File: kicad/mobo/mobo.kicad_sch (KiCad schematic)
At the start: 9 parts, among them J1 nice!view, J12 columns, J2 Battery, J4 sensor, J8 rgb, J9 rows, SW1 Power, SW2 Reset, U1 nice!nano v2

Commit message: Dumping everything i need into the combined schematic
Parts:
- removed J1: nice!view, Connector_PinHeader_2.54mm:PinHeader_1x05_P2.54mm_Vertical, symbol Connector:Conn_01x05_Socket
- removed U1: nice!nano v2, ScottoKeebs_MCU:Nice_Nano_V2_Flipped, symbol ScottoKeebs:MCU_Nice_Nano_V2
- added C1: 560pF/680pF, Capacitor_SMD:C_0603_1608Metric_Pad1.08x0.95mm_HandSolder, symbol Device:C_Small
- added C1, C17: 100n, Capacitor_SMD:C_0402_1005Metric, symbol Device:C_Small
- added C12: 1u, Capacitor_SMD:C_0402_1005Metric, symbol Device:C_Small
- added C13, C14, C5, C6, C7: 4u7, Capacitor_SMD:C_0402_1005Metric, symbol Device:C_Small
- added C15, C16: 12p, Capacitor_SMD:C_0402_1005Metric, symbol Device:C_Small
- added C2, C3: 1uF, Capacitor_SMD:C_0603_1608Metric_Pad1.08x0.95mm_HandSolder, symbol Device:C_Small
- added D1: BSD3C051V, Diode_SMD:D_SOD-323, symbol Device:D_TVS
- added F1: 750 mA, Fuse:Fuse_0603_1608Metric, symbol Device:Fuse_Small
- added FB1, FB2: Ferrite_Bead_Small, Resistor_SMD:R_0805_2012Metric_Pad1.20x1.40mm_HandSolder, symbol sharp_memory_display-rescue:Ferrite_Bead_Small-Device
- added J1: Conn_01x05, Connector_PinSocket_2.54mm:PinSocket_1x05_P2.54mm_Vertical, symbol Connector_Generic:Conn_01x05
- added J10: TC2030_SWD, PCM_marbastlib-various:CON_TC2030_outlined, symbol PCM_marbastlib-various:TC2030_SWD
- added J2: HRO_TYPE-C-31-M-14, Connector_USB:USB_C_Receptacle_HRO_TYPE-C-31-M-12, symbol Connector:USB_C_Receptacle_USB2.0
- added J2: Conn_01x10, Connector_FFC-FPC:Hirose_FH12-10S-0.5SH_1x10-1MP_P0.50mm_Horizontal, symbol Connector_Generic:Conn_01x10
- added J3: Battery, PCM_marbastlib-various:Molex_Pico-EZmate_78171-0002_1x02-1MP_P1.20mm_Vertical, symbol Connector_Generic_MountingPin:Conn_01x02_MountingPin
- added L1, L2: BLM15PX121SN1D, Inductor_SMD:L_0402_1005Metric, symbol Device:L_Small
- added L3: 10 uH, Inductor_SMD:L_0603_1608Metric, symbol Device:L_Small
- added LED2: orange, LED_SMD:LED_0402_1005Metric, symbol Device:LED_Small
- added Q2, Q4: 2N7002, Package_TO_SOT_SMD:SOT-23, symbol Transistor_FET:2N7002
- added Q3: AO3401A, Package_TO_SOT_SMD:SOT-23, symbol Transistor_FET:AO3401A
- added R1, R2, R3: 10k, Resistor_SMD:R_0603_1608Metric_Pad0.98x0.95mm_HandSolder, symbol Device:R_Small
- added R1, R18, R19, R2: 5k1, Resistor_SMD:R_0402_1005Metric, symbol Device:R_Small
- added R10, R12: 1k5, Resistor_SMD:R_0402_1005Metric, symbol Device:R_Small
- added R11: 47k, Resistor_SMD:R_0402_1005Metric, symbol Device:R_Small
- added R13: 3k9, Resistor_SMD:R_0402_1005Metric, symbol Device:R_Small
- added R23, R25, R7, R9: 10k, Resistor_SMD:R_0402_1005Metric, symbol Device:R_Small
- added R24, R4: 100R, Resistor_SMD:R_0402_1005Metric, symbol Device:R_Small
- added R3: 100k, Resistor_SMD:R_0402_1005Metric, symbol Device:R_Small
- added SW1: PWR, PCM_marbastlib-various:SW_MSK12C02-HB, symbol Switch:SW_Push_SPDT
- added U1: SRV05-4, Package_TO_SOT_SMD:SOT-23-6, symbol Power_Protection:SRV05-4
- added U10: MAX17048, Package_DFN_QFN:DFN-8-1EP_2x2mm_P0.5mm_EP0.7x1.3mm, symbol marbastlib-various:MAX17048
- added U3: BQ24075, Package_DFN_QFN:VQFN-16-1EP_3x3mm_P0.5mm_EP1.6x1.6mm, symbol Battery_Management:BQ24075RGT
- added U9: nRF52840_E73-2G4M08S1C, E73-2G4M08S1C Model:E73-2G4M08S1C, symbol PCM_marbastlib-various:nRF52840_E73-2G4M08S1C
- added Y1: 32.768 KHz, Crystal:Crystal_SMD_2012-2Pin_2.0x1.2mm, symbol Device:Crystal_Small
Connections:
- net GND: now also C1.2, C1.2, C12.2, C13.2, C14.2, C15.2, C16.2, C17.1, C3.2, C5.2, C6.2, C7.2, D1.1 (A1), FB2.1, J1.1 (Pin_1), J10.5 (GND), J2.9 (Pin_9), J3.2 (Pin_2), J3.MP (MountPin), L2.2, Q2.2 (S), Q4.2 (S), R1.2, R11.2, R12.2, R13.2, R2.2, R25.2, R7.2, R9.2, SW1.3 (C), U1.2 (VN), U10.1 (CTG), U10.4 (GND), U10.6 (QSTRT), U10.9 (GND), U3.17 (VSS), U3.4 (~{CE}), U3.5 (EN2), U3.8 (VSS), U9.21 (GND), U9.24 (GND), U9.5 (GND)
- net RST: now also J10.3 (~{RST}), U9.26 (P0.18/~{RESET})
- net VCC: no longer J8.3 (Pin_3)
- new net: C15.1, U9.11 (P0.00/XL1), Y1.2
- new net: C16.1, U9.13 (P0.01/XL2), Y1.1
- new net: Q4.1 (G), R24.2, R25.1
- new net: F1.1, L1.2
- new net: Q3.1 (G), Q4.3 (D), R23.2
- new net: R9.1, U3.1 (TS)
- new net: R13.1, U3.16 (ISET)
- new net: R10.2, U3.9 (~{CHG})
- new net: LED2.1 (K), R10.1
- new net: Q2.1 (G), R4.2, R7.1
- new net: J2.A5 (CC1), R2.2
- new net: J2.B5 (CC2), R1.2
- new net: R3.1, SW1.1 (A)
- new net +3.3V: C12.1, C3.1, FB1.2, J1.2 (Pin_2), J10.1 (VCC), J2.7 (Pin_7), L3.2, R18.2, R19.2, R3.1, U9.19 (VDD)
- new net +5V: C13.1, C5.1, F1.2, R4.1, U1.5 (VP), U3.13 (IN), U9.27 (VBUS)
- new net +BATT: C17.2, C7.1, J3.1 (Pin_1), R3.2, U10.2 (CELL), U10.3 (VDD), U3.2 (BAT), U3.3 (BAT)
- new net +VSW: C14.1, C6.1, LED2.2 (A), Q3.2 (S), R23.1, U3.10 (OUT), U3.11 (OUT), U3.6 (EN1), U9.23 (VDDH)
- new net ALERT: U10.5 (~{ALRT})
- new net DCCH: L3.1, U9.25 (DCCH)
- new net DISP: C1.1, J2.5 (Pin_5), R3.2
- new net EXTCOMIN: J2.4 (Pin_4), R2.1
- new net EXTMODE: J2.8 (Pin_8), R1.1
- new net Earth: C1.1, D1.2 (A2), J2.A1 (GND), J2.A12 (GND), J2.B1 (GND), J2.B12 (GND), J2.S1 (SHIELD), L2.1
- new net GNDA: C2.2, FB2.2, J2.10 (Pin_10)
- new net GNDPWR: R1.1, R2.1
- new net ILIM: R12.1, U3.12 (ILIM)
- new net SCL: R19.1, U10.7 (SCL), U9.15 (P0.05/AIN3)
- new net SCLK: J1.5 (Pin_5), J2.1 (Pin_1)
- new net SCS: J1.3 (Pin_3), J2.3 (Pin_3)
- new net SDA: R18.1, U10.8 (SDA), U9.22 (P0.07)
- new net SI: J1.4 (Pin_4), J2.2 (Pin_2)
- new net SWDCLK: J10.4 (SWCLK), U9.39 (SWDCLK)
- new net SWDIO: J10.2 (SWDIO), U9.37 (SWDIO)
- new net SYSOFF: Q2.3 (D), SW1.2 (B), U3.15 (SYSOFF)
- new net TMR: R11.1, U3.14 (TMR)
- new net UG_EN: R24.1, U9.36 (P1.00)
- new net UG_LV: U9.34 (P0.22)
- new net UG_PWR: J8.3 (Pin_3), Q3.3 (D)
- new net USB-D+: J2.A6 (D+), J2.B6 (D+), U1.6 (IO4), U9.31 (D+)
- new net USB-D-: J2.A7 (D-), J2.B7 (D-), U1.1 (IO1), U9.29 (D-)
- new net VBUS: J2.A4 (VBUS), J2.A9 (VBUS), J2.B4 (VBUS), J2.B9 (VBUS), L1.1
- new net VDDA: C2.1, FB1.1, J2.6 (Pin_6)
- new net col0: U9.7 (P0.02/AIN0)
- new net col1: U9.4 (P0.28/AIN4)
- new net row0: U9.8 (P0.29/AIN5)
- new net row1: U9.10 (P0.30/AIN6)
- no-connect marks 0 -> 6
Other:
- note added: "Battery management (advanced)"
- note added: "External DCCH inductor for DC-DC HV input mode"
- note added: "External LF crystal for lower idle power"
- note added: "IO connectors"
- note added: "LCD Screen"
- note added: "MCU section (ebyte E73-2G4M08S1C)"
- note added: "SYSOFF 1 (SW1 pos 1): Batt OFF SYSOFF 0 (SW1 pos 3): Batt ON"
- note added: "TMR: (10 x 48 s/kOhm) * 47 kOhm = 22560s = 6.27h ILIM: 1550 AOhm / 1500 Ohm = 1.03 A = 1030 mA ISET: 890 AOhm / 3900 Ohm = 0.228 A = 230 mA EN1: 1, EN2: 0 = 475 mA MAX TS: 10 kOhm to GND = no OTP"
- note added: "USB connectors and protections"
- note added: "Underglow enable"
- note added: "Voltage sensing (advanced)"
- moved on the sheet: J12, J2, J4, J8, J9, SW1, SW2

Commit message: Cleaning up the schematics
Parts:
- removed C1, C17: 100n, Capacitor_SMD:C_0402_1005Metric, symbol Device:C_Small
- removed D1: BSD3C051V, Diode_SMD:D_SOD-323, symbol Device:D_TVS
- removed F1: 750 mA, Fuse:Fuse_0603_1608Metric, symbol Device:Fuse_Small
- removed J1: Conn_01x05, Connector_PinSocket_2.54mm:PinSocket_1x05_P2.54mm_Vertical, symbol Connector_Generic:Conn_01x05
- removed J10: TC2030_SWD, PCM_marbastlib-various:CON_TC2030_outlined, symbol PCM_marbastlib-various:TC2030_SWD
- removed J3: Battery, PCM_marbastlib-various:Molex_Pico-EZmate_78171-0002_1x02-1MP_P1.20mm_Vertical, symbol Connector_Generic_MountingPin:Conn_01x02_MountingPin
- removed L1, L2: BLM15PX121SN1D, Inductor_SMD:L_0402_1005Metric, symbol Device:L_Small
- removed Q2: 2N7002, Package_TO_SOT_SMD:SOT-23, symbol Transistor_FET:2N7002
- removed R18, R19: 5k1, Resistor_SMD:R_0402_1005Metric, symbol Device:R_Small
- removed R3: 100k, Resistor_SMD:R_0402_1005Metric, symbol Device:R_Small
- removed R4: 100R, Resistor_SMD:R_0402_1005Metric, symbol Device:R_Small
- removed R7: 10k, Resistor_SMD:R_0402_1005Metric, symbol Device:R_Small
- removed SW1: Power, Button_Switch_SMD:SW_SPDT_PCM12, symbol ScottoKeebs:Placeholder_Switch
- removed SW1: PWR, PCM_marbastlib-various:SW_MSK12C02-HB, symbol Switch:SW_Push_SPDT
- removed U1: SRV05-4, Package_TO_SOT_SMD:SOT-23-6, symbol Power_Protection:SRV05-4
- removed U10: MAX17048, Package_DFN_QFN:DFN-8-1EP_2x2mm_P0.5mm_EP0.7x1.3mm, symbol marbastlib-various:MAX17048
- added R11, R14, R15, R16, R8: 100R, Resistor_SMD:R_0402_1005Metric, symbol Device:R_Small
- added SW1: Battery, symbol Switch:SW_SPST
- J4: renamed from J12; symbol Connector:Conn_01x07_Socket -> Connector:Conn_01x06_Socket
- J6: renamed from J9; symbol Connector:Conn_01x04_Socket -> Connector:Conn_01x05_Socket
- renumbered C5 to C1, C2 to C10, C16 to C11, C6 to C2, C7 to C3, C12 to C4, C13 to C5, C14 to C6, C1 to C7, C3 to C8, C15 to C9, J2 to J1, J8 to J3, J2 to J5, J4 to J7, L3 to L1, LED2 to LED1, Q3 to Q1, Q4 to Q2, R2 to R1, R23 to R10, R1 to R12, R2 to R13, R24 to R17, R25 to R18, R1 to R2, R9 to R3, R10 to R4, R11 to R5, R12 to R6, R13 to R7, R3 to R9, U3 to U1, U9 to U2
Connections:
- net GNDPWR is gone; now on net GND: R1.1, R2.1
- net VBUS is gone; now on net +5V: J1.A4 (VBUS), J1.A9 (VBUS), J1.B4 (VBUS), J1.B9 (VBUS)
- net VCC is gone; now on net +3.3V: J7.1 (Pin_1)
- net +BATT: now also SW1.2 (B)
- net GND: now also J1.A1 (GND), J1.A12 (GND), J1.B1 (GND), J1.B12 (GND), J2.2 (Pin_2), J3.3 (Pin_3); no longer J2.1 (Pin_1), J3.2 (Pin_2)
- net CS_T: no longer names the net of J7.2 (Pin_2)
- net CS_T: now also R11.2
- removed net Col 6: J4.7 (Pin_7)
- net DISP: no longer names the net of C7.1, J5.5 (Pin_5), R9.2
- removed net Earth: J1.A1 (GND), J1.A12 (GND), J1.B1 (GND), J1.B12 (GND), J1.S1 (SHIELD)
- net IRQ: no longer names the net of J7.5 (Pin_5)
- net IRQ: now also R16.2
- net RGB renamed RGB_PWR
- net RGB_PWR: now also Q1.3 (D)
- net SCK: no longer names the net of J7.4 (Pin_4)
- net SCK: now also R15.2
- net SCL: no longer names the net of U2.15 (P0.05/AIN3)
- net SCLK renamed LCD_CLK
- net SCS renamed LCD_CS
- net SDA: no longer names the net of U2.22 (P0.07)
- net SDIO: no longer names the net of J7.3 (Pin_3)
- net SDIO: now also R14.2
- net SI renamed LCD_IN
- net SWDCLK: no longer names the net of U2.39 (SWDCLK)
- net SWDIO: no longer names the net of U2.37 (SWDIO)
- net SYSOFF: no longer names the net of U1.15 (SYSOFF)
- net UG_EN renamed RGB_ON
- net UG_LV: no longer names the net of U2.34 (P0.22)
- removed net UG_PWR: J3.3 (Pin_3), Q1.3 (D)
- net col0: no longer names the net of U2.7 (P0.02/AIN0)
- net col1: no longer names the net of U2.4 (P0.28/AIN4)
- net row0: no longer names the net of U2.8 (P0.29/AIN5)
- net row1: no longer names the net of U2.10 (P0.30/AIN6)
- new net: J2.1 (Pin_1), SW1.1 (A)
- new net: J3.2 (Pin_2), R8.2
- new net RGB_DATA: R8.1
- new net Row 4: J6.5 (Pin_5)
- new net SENSOR_IRQ: R16.1
- new net SENSOR_SCK: R15.1
- new net SENSOR_SDIO: R14.1
- new net SESOR_CS: R11.1
- no-connect marks 6 -> 5
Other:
- note added: "Battery management"
- note added: "MCU section"
- note added: "USB connector"
- note removed: "Battery management (advanced)"
- note removed: "MCU section (ebyte E73-2G4M08S1C)"
- note removed: "SYSOFF 1 (SW1 pos 1): Batt OFF SYSOFF 0 (SW1 pos 3): Batt ON"
- note removed: "USB connectors and protections"
- note removed: "Voltage sensing (advanced)"
- moved on the sheet: C1, C2, C3, J1, J2, J3, J7, LED1, R1, R2, R3, R4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

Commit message: Replacing the through holes with JST-SH connectors
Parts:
- J2: footprint Connector_JST:JST_ZH_S2B-ZR-SM4A-TF_1x02-1MP_P1.50mm_Horizontal -> Connector_JST:JST_SH_SM02B-SRSS-TB_1x02-1MP_P1.00mm_Horizontal
- J3: footprint Connector_Wuerth:Wuerth_WR-WTB_64800311622_1x03_P1.50mm_Vertical -> Connector_JST:JST_SH_SM03B-SRSS-TB_1x03-1MP_P1.00mm_Horizontal
- J4: footprint Connector_Wuerth:Wuerth_WR-WTB_64800711622_1x07_P1.50mm_Vertical -> Connector_JST:JST_SH_SM06B-SRSS-TB_1x06-1MP_P1.00mm_Horizontal
- J6: footprint Connector_Wuerth:Wuerth_WR-WTB_64800411622_1x04_P1.50mm_Vertical -> Connector_JST:JST_SH_SM05B-SRSS-TB_1x05-1MP_P1.00mm_Horizontal
- J7: footprint Connector_Wuerth:Wuerth_WR-WTB_64800611622_1x06_P1.50mm_Vertical -> Connector_JST:JST_SH_SM06B-SRSS-TB_1x06-1MP_P1.00mm_Horizontal
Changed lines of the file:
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@@
 			)
 		)
-		(property "Footprint" "Connector_Wuerth:Wuerth_WR-WTB_64800711622_1x07_P1.50mm_Vertical"
+		(property "Footprint" "Connector_JST:JST_SH_SM06B-SRSS-TB_1x06-1MP_P1.00mm_Horizontal"
 			(at 223.52 143.51 0)
 			(effects
@@
 			)
 		)
-		(property "Footprint" "Connector_JST:JST_ZH_S2B-ZR-SM4A-TF_1x02-1MP_P1.50mm_Horizontal"
+		(property "Footprint" "Connector_JST:JST_SH_SM02B-SRSS-TB_1x02-1MP_P1.00mm_Horizontal"
 			(at 193.04 62.23 0)
 			(effects
@@
 			)
 		)
-		(property "Footprint" "Connector_Wuerth:Wuerth_WR-WTB_64800311622_1x03_P1.50mm_Vertical"
+		(property "Footprint" "Connector_JST:JST_SH_SM03B-SRSS-TB_1x03-1MP_P1.00mm_Horizontal"
 			(at 224.79 127 0)
 			(effects
@@
 			)
 		)
-		(property "Footprint" "Connector_Wuerth:Wuerth_WR-WTB_64800411622_1x04_P1.50mm_Vertical"
+		(property "Footprint" "Connector_JST:JST_SH_SM05B-SRSS-TB_1x05-1MP_P1.00mm_Horizontal"
 			(at 223.52 162.56 0)
 			(effects
@@
 			)
 		)
-		(property "Footprint" "Connector_Wuerth:Wuerth_WR-WTB_64800611622_1x06_P1.50mm_Vertical"
+		(property "Footprint" "Connector_JST:JST_SH_SM06B-SRSS-TB_1x06-1MP_P1.00mm_Horizontal"
 			(at 223.52 187.96 0)
 			(effects

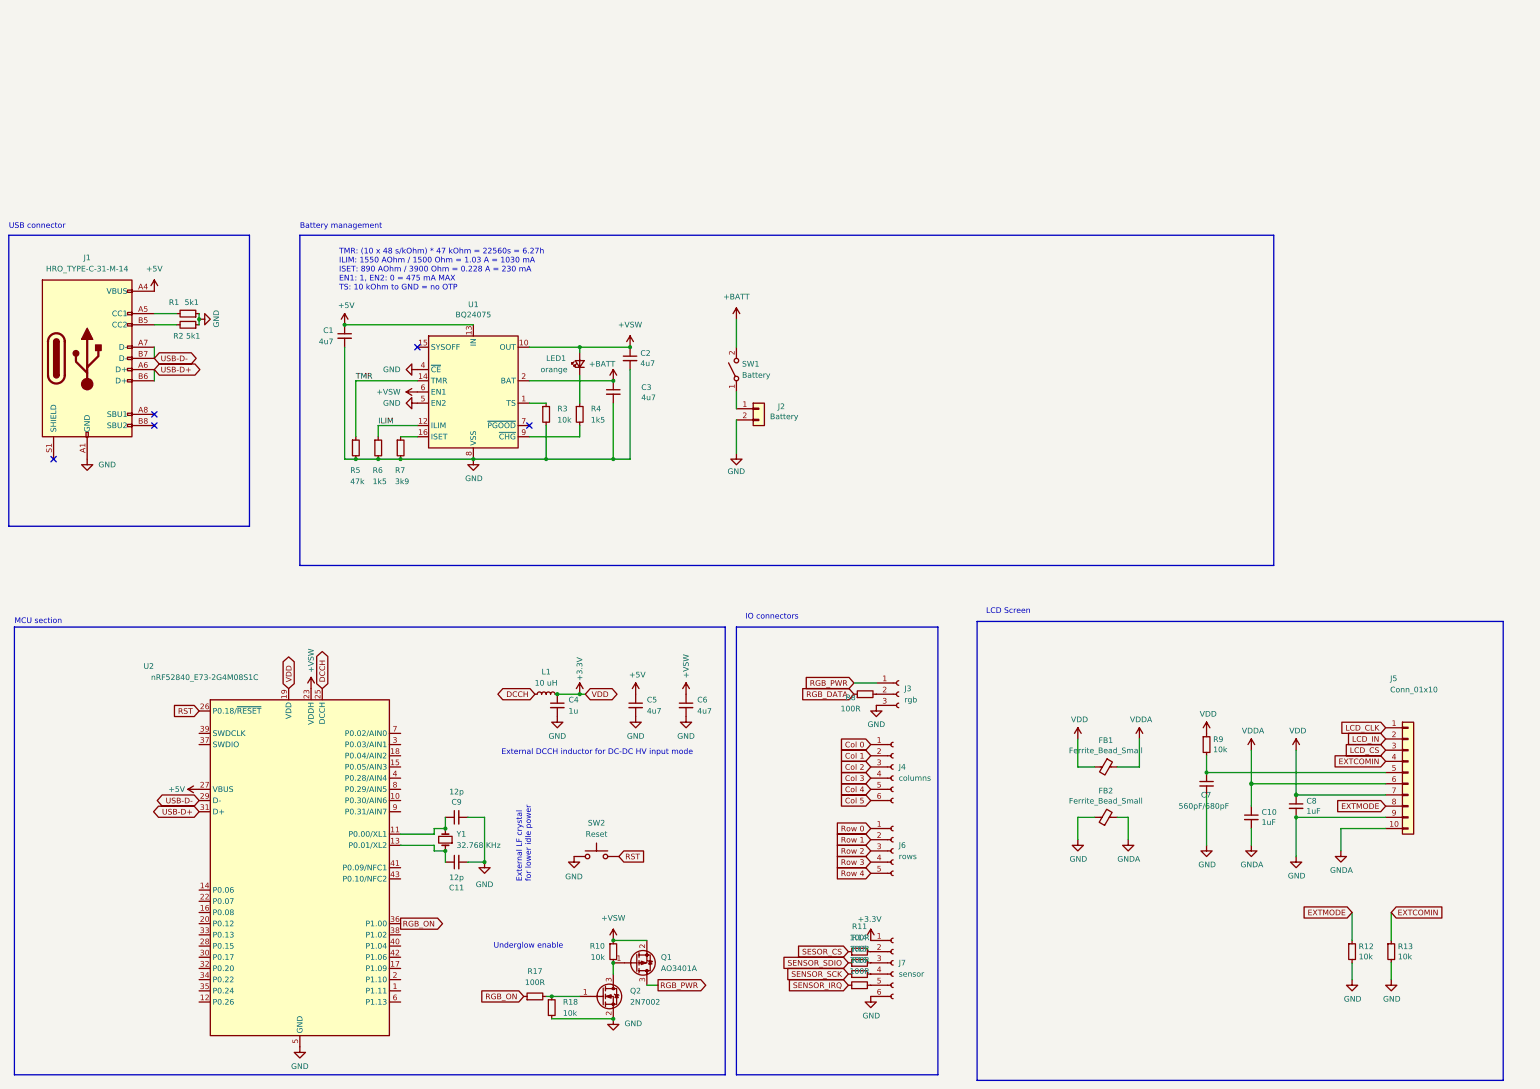
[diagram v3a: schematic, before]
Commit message: Assigning all the perifery pins
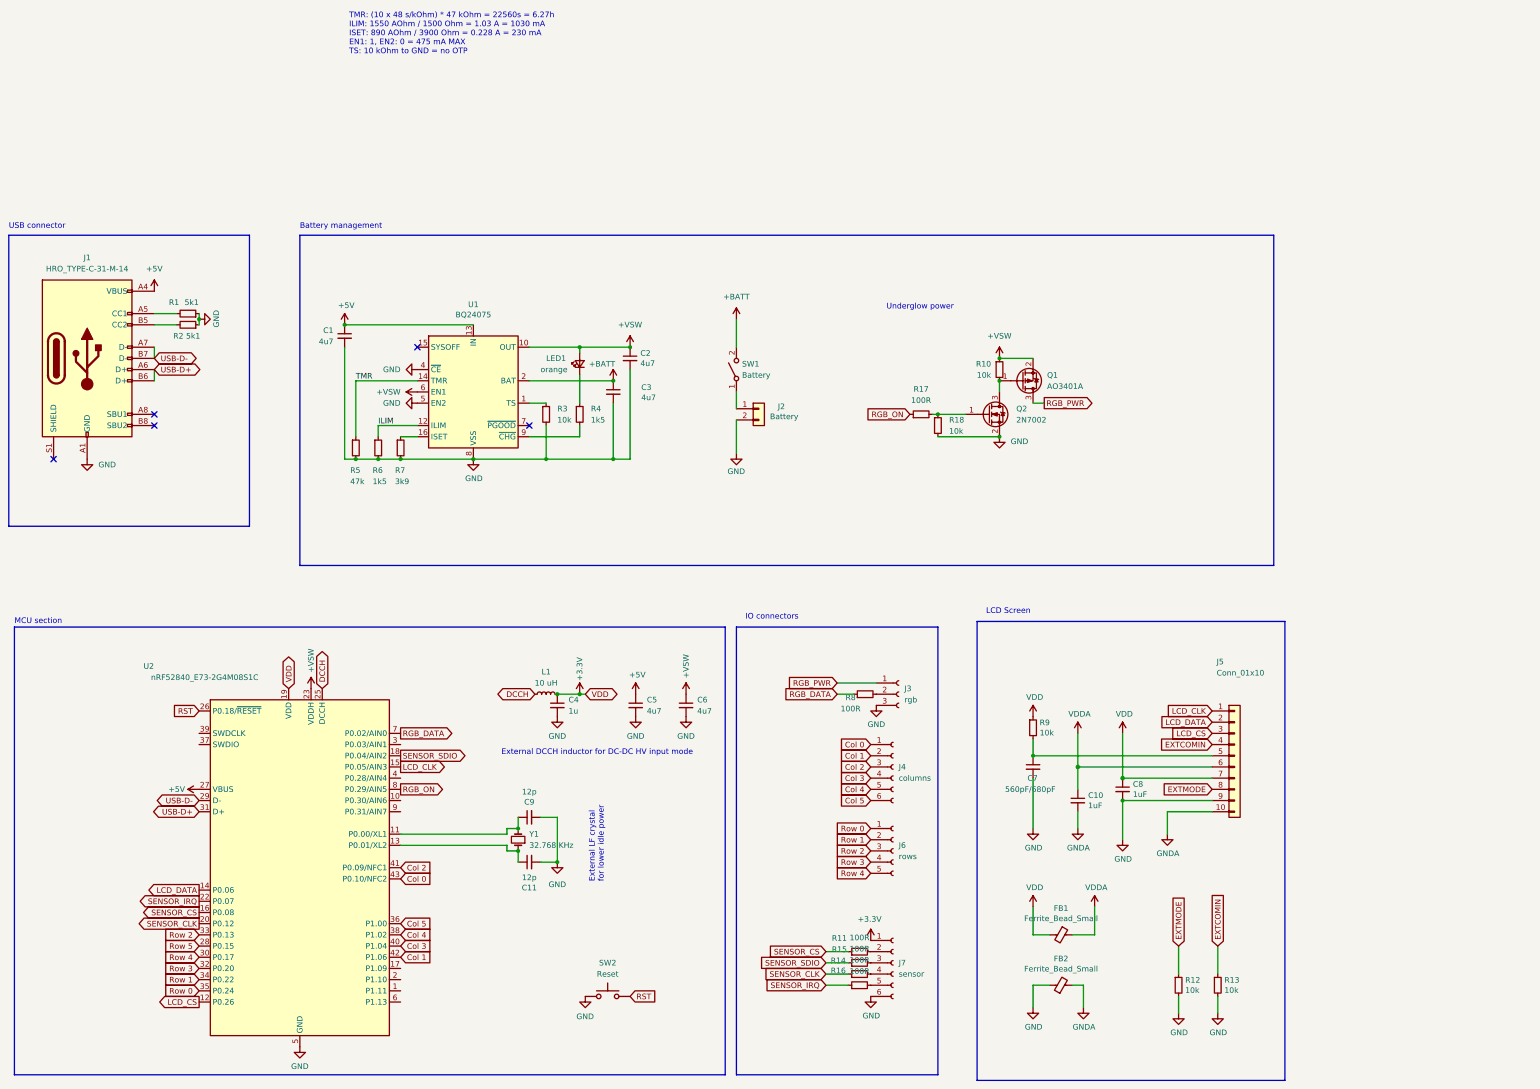
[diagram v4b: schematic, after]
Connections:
- net LCD_IN is gone; now on net LCD_DATA: J5.2 (Pin_2)
- net SENSOR_SCK is gone; now on net SENSOR_CLK: R15.1
- net SESOR_CS is gone; now on net SENSOR_CS: R11.1
- net Col 0: now also U2.43 (P0.10/NFC2)
- net Col 1: now also U2.42 (P1.06)
- net Col 2: now also U2.41 (P0.09/NFC1)
- net Col 3: now also U2.40 (P1.04)
- net Col 4: now also U2.38 (P1.02)
- net Col 5: now also U2.36 (P1.00)
- net LCD_CLK: now also U2.15 (P0.05/AIN3)
- net LCD_CS: now also U2.12 (P0.26)
- net RGB_DATA: now also U2.7 (P0.02/AIN0)
- net RGB_ON: now also U2.8 (P0.29/AIN5); no longer U2.36 (P1.00)
- net Row 0: now also U2.35 (P0.24)
- net Row 1: now also U2.34 (P0.22)
- net Row 2: now also U2.33 (P0.13)
- net Row 3: now also U2.32 (P0.20)
- net Row 4: now also U2.30 (P0.17)
- net SENSOR_IRQ: now also U2.22 (P0.07)
- net SENSOR_SDIO: now also U2.18 (P0.04/AIN2)
- net LCD_DATA: now reaches U2.14 (P0.06)
- net SENSOR_CS: now reaches U2.16 (P0.08)
- net SENSOR_CLK: now reaches U2.20 (P0.12)
- net Row 5: now reaches U2.28 (P0.15)
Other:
- note added: "Underglow power"
- note removed: "Underglow enable"
- moved on the sheet: C10, C11, C7, C8, C9, FB1, FB2, J5, Q1, Q2, R10, R12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

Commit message: Loosely optimising the groups components placement
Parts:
- FB1, FB2: value Ferrite_Bead_Small -> 2.7k
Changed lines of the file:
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@@
 			)
 		)
-		(property "Value" "Ferrite_Bead_Small"
+		(property "Value" "2.7k"
 			(at 261.62 189.3316 90)
 			(effects
@@
 		(on_board yes)
 		(dnp no)
+		(fields_autoplaced yes)
 		(property "Reference" "FB1"
-			(at 261.62 175.5902 90)
+			(at 261.6581 175.26 90)
 			(effects
 				(font
@@
 			)
 		)
-		(property "Value" "Ferrite_Bead_Small"
-			(at 261.62 177.9016 90)
+		(property "Value" "2.7k"
+			(at 261.6581 177.8 90)
 			(effects
 				(font
